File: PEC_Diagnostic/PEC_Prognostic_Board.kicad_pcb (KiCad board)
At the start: 4 copper layers, 29 parts, among them J1 Conn_2Rows-21Pins, U1 SHT40_Digital_Humidity_Sensor, U10 ACS712, U11 ACS712, U12 ACS712, U2 MPU-6050_Inertial_Measurement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, U3 TI_INA219_Voltage_Reader, U4 TI_INA219_Voltage_Reader, U5 TI_INA219_Voltage_Reader, U6 TI_INA219_Voltage_Reader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

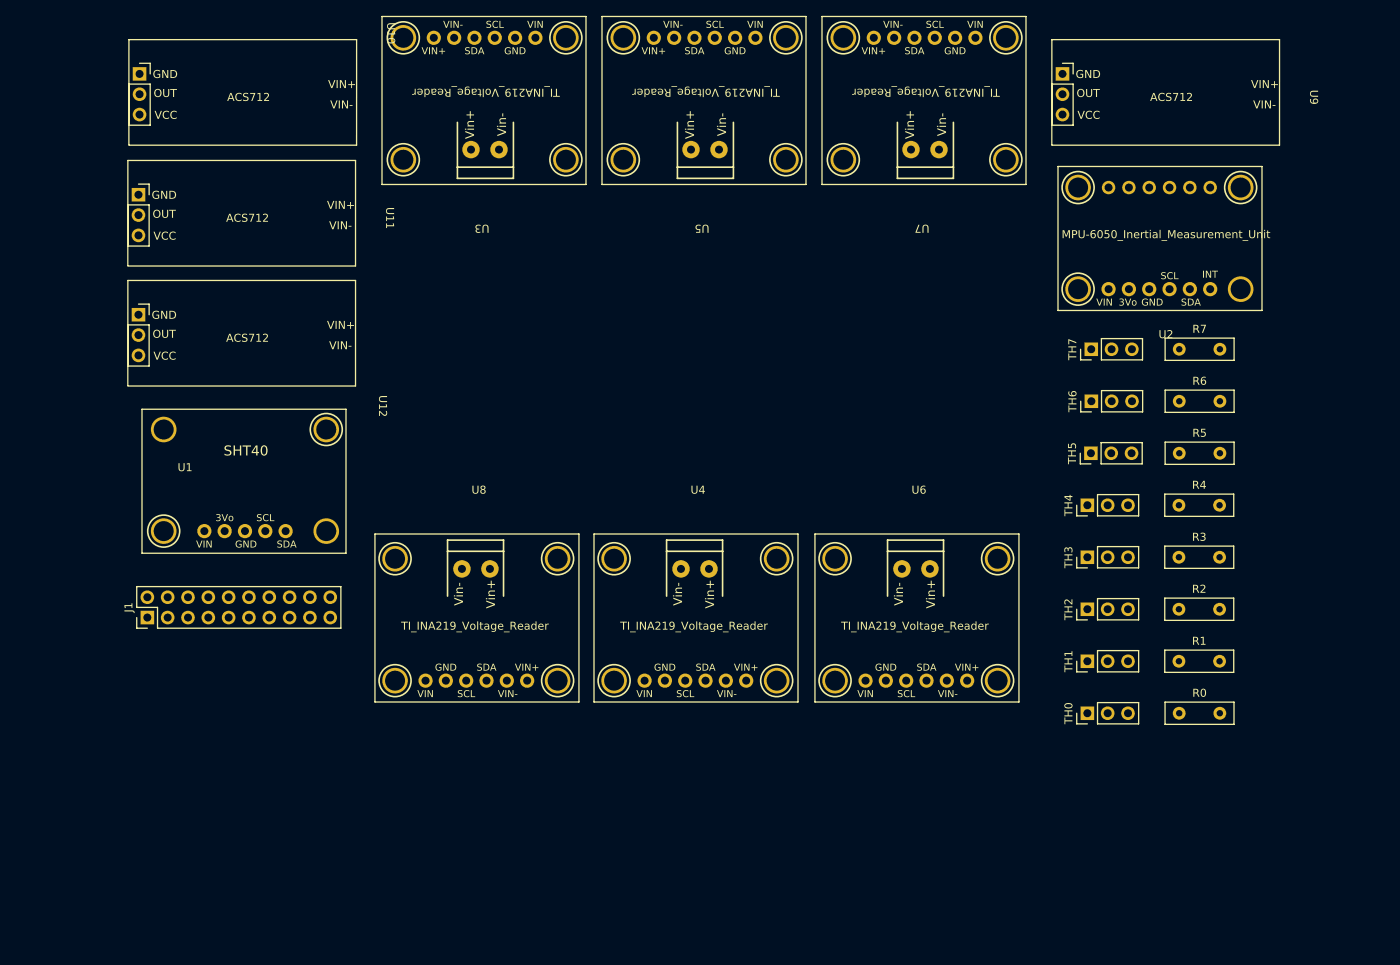
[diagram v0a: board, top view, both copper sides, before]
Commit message: PCB Updated
Set stackup layers
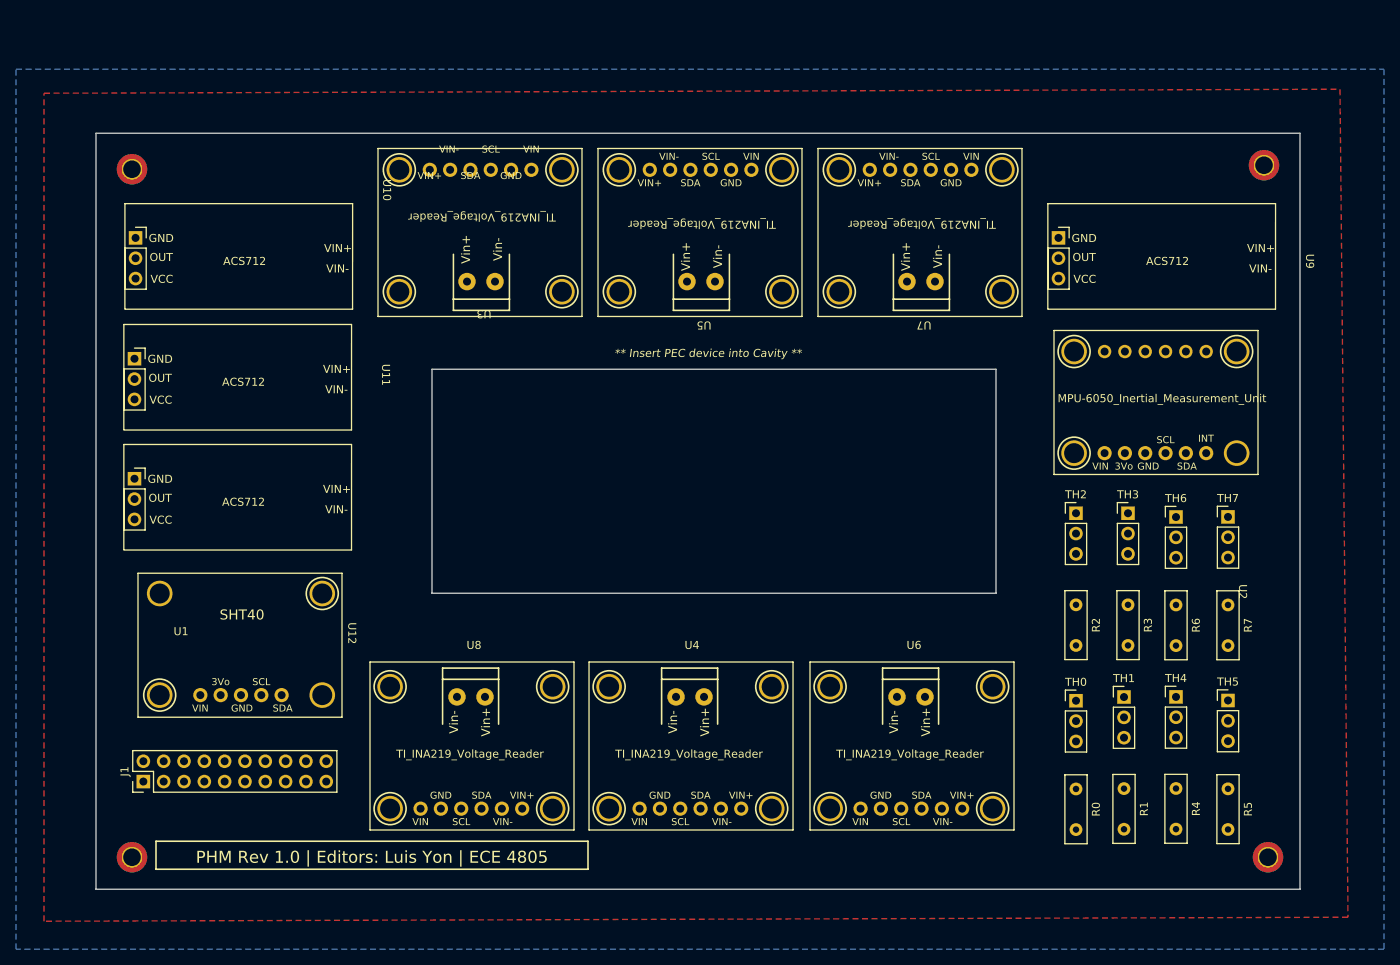
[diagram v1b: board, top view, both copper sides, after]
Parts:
- added REF**: MountingHole_2.2mm_M2_DIN965_Pad_TopBottom, MountingHole:MountingHole_2.2mm_M2_DIN965_Pad_TopBottom, F.Cu at (216.0, 130.5)
- added REF**: MountingHole_2.2mm_M2_DIN965_Pad_TopBottom, MountingHole:MountingHole_2.2mm_M2_DIN965_Pad_TopBottom, F.Cu at (74.0, 44.5)
- added REF**: MountingHole_2.2mm_M2_DIN965_Pad_TopBottom, MountingHole:MountingHole_2.2mm_M2_DIN965_Pad_TopBottom, F.Cu at (74.0, 130.5)
- added REF**: MountingHole_2.2mm_M2_DIN965_Pad_TopBottom, MountingHole:MountingHole_2.2mm_M2_DIN965_Pad_TopBottom, F.Cu at (215.5, 44.0)
- moved R5 42.4 mm to (211.0, 122.0), turned to -90 degrees
- moved R4 35.4 mm to (204.5, 121.9), turned to -90 degrees
- moved TH5 35.3 mm to (211.0, 110.9), turned to 0 degrees
- moved R7 32.5 mm to (211.0, 99.0), turned to -90 degrees
- moved TH7 27.0 mm to (211.0, 88.0), turned to 0 degrees
- moved TH4 26.4 mm to (204.5, 110.5), turned to 0 degrees
- moved R6 25.5 mm to (204.5, 99.0), turned to -90 degrees
- moved J1 20.5 mm to (75.4, 121.0)
- moved U1 20.5 mm to (87.8, 104.7)
- moved U10 20.5 mm to (83.0, 56.0)
- moved U12 20.5 mm to (82.9, 86.1)
- moved U2 20.5 mm to (202.8, 86.2)
- moved U9 20.5 mm to (198.4, 56.0)
- moved U11 20.5 mm to (82.9, 71.1)
- moved TH6 17.9 mm to (204.5, 88.0), turned to 0 degrees
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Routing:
- added copper zone on B.Cu, net (none)
- added copper zone on F.Cu, net (none)
- added copper zone on In1.Cu, net +5V
- added copper zone on In2.Cu, net GND
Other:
- board outline added: 150.5 x 94.5 mm
- board text added: "** Insert PEC device into Cavity **"
- board text added: "PHM Rev 1.0 | Editors: Luis Yon | ECE 4805"
